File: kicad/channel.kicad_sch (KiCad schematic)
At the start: 20 parts, among them U1 OPA1678IDR

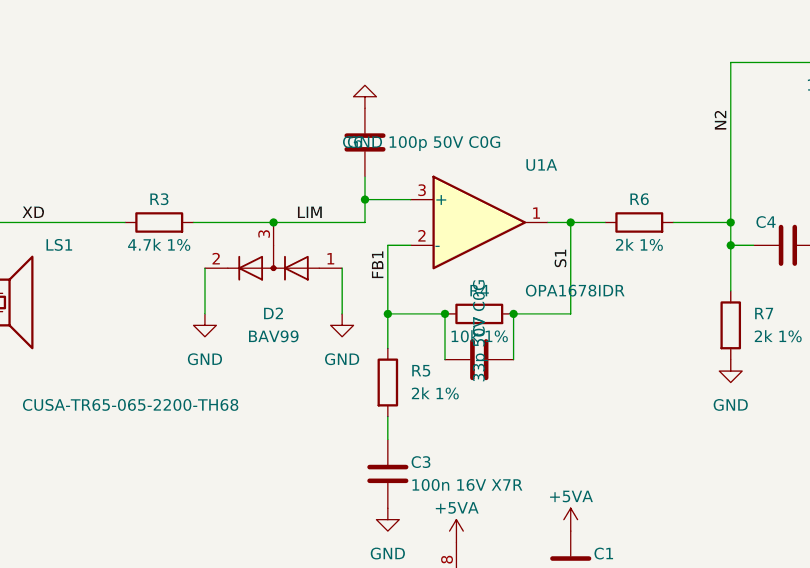
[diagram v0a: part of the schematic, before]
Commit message: AD7606C-16, one sheet per repeated block, clock buffering, first simulations
- ADC: AD7606C-16 in software mode (OS pins high, WR held high, DB11/SDI on
  shared ADC_SDI), 33 R source resistors on DOUTA/DOUTB/BUSY.
- Every repeated block is its own reused sheet: tx_group x16, en_buf x4,
  clk_buf x7, mic x8 (replaces tx_shift, tx_drivers, mems). Sheets other than
  channel are generated by scripts/build_cells.py and scripts/build_power.py.
- Headers: GND conductors either side of every clock, ADC_SDI, idle pulls,
  DNP RC terminations as fallback.
- Power: 3V3_MIC ferrite filter moved to the power sheet with LED, test point
  and flag.
- Simulations (LTspice, sim/): RX chain gain/noise, TX burst and recovery,
  clock signal integrity; results in docs/simulation-1.md. FPGA ribbon outputs
  changed to DRIVE 4 after simulation.
- Brief, CLAUDE.md, review status and SKiDL reference spec updated.
  ERC: 0 violations, 1,701 parts.
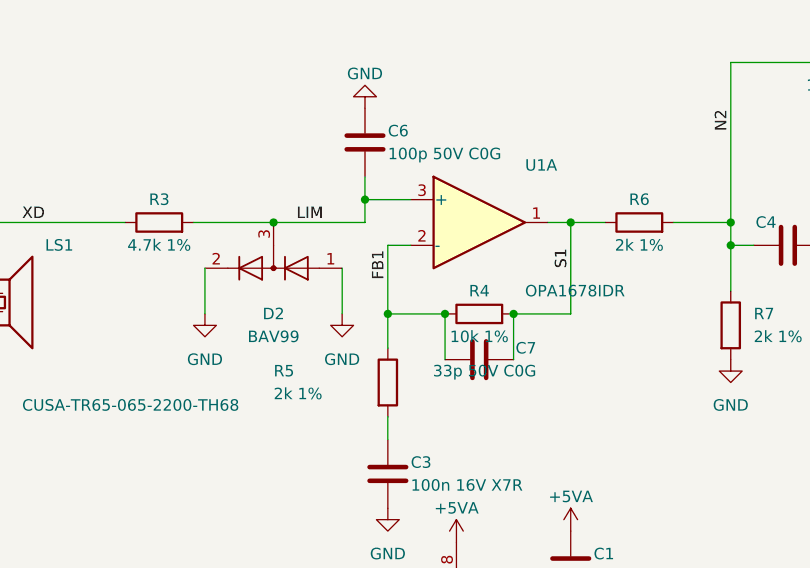
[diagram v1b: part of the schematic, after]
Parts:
- C6, C7: LCSC (none) -> TBD

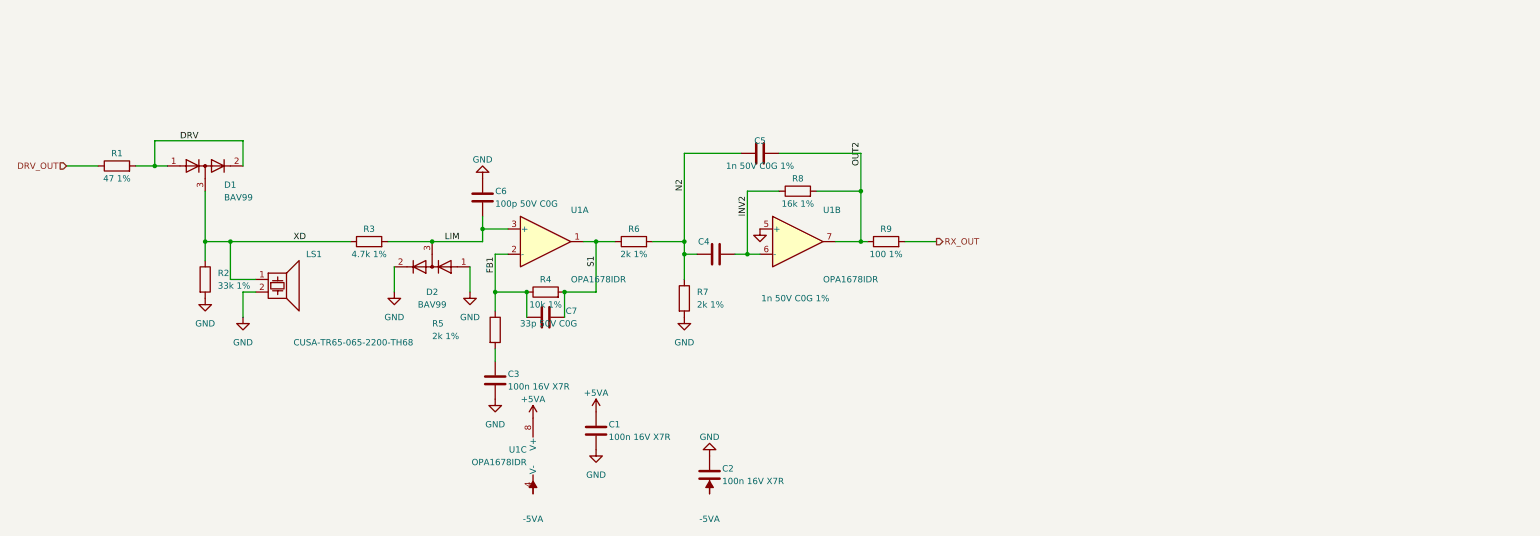
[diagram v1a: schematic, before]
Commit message: Block-diagram top page, power review fixes, readable sheets
Top level
- Page 1 is now a block diagram of the signal flow (FPGA -> headers ->
  clock buffers / TX drive -> transceivers -> ADCs -> FPGA, mics, power).
- New group sheets hold the reused cells: tx (16 tx_group + 4 en_buf),
  array (64 channel), adcs (8 adc), mics (8 mic), clocks (7 clk_buf).
  Power and headers stay directly under the top. All written by gen_top.py,
  which now also survives a kicad-cli re-save of a cell sheet.

Power (review findings)
- Polyfuse 1812L200/16DR (16 V), TPS65131RGER stated explicitly, input caps
  2 x 10u 1206, 50 V caps on 12 V, inductor values carry minimum Isat.
- +3V3: TLV75733P (ceramic-stable) replaces TLV1117-33.
- New JP5/JP6 isolate +-6V5; every rail: REG node -> jumper -> rail with TP,
  LED (not on analog LDOs) and PWR_FLAG.
- Power sheet is now generated by build_cells.py in a 2x3 block layout
  (build_power.py removed).

Readability and small fixes
- Rails on sideways pins use labelled flags; sideways GND symbols hide text.
- tx_group: 595 outputs wired straight to the drivers.
- Title blocks on every sheet; channel sheet notes and field placement fixed
  (sch_fields.py --only, sch_annotate.py).
- ADC_SDI 10k pull-down, ADC reset/DOUT notes, mic cap 50 V.
- ERC 0 violations, 1,704 parts. PDFs: docs/schematics/00..13.
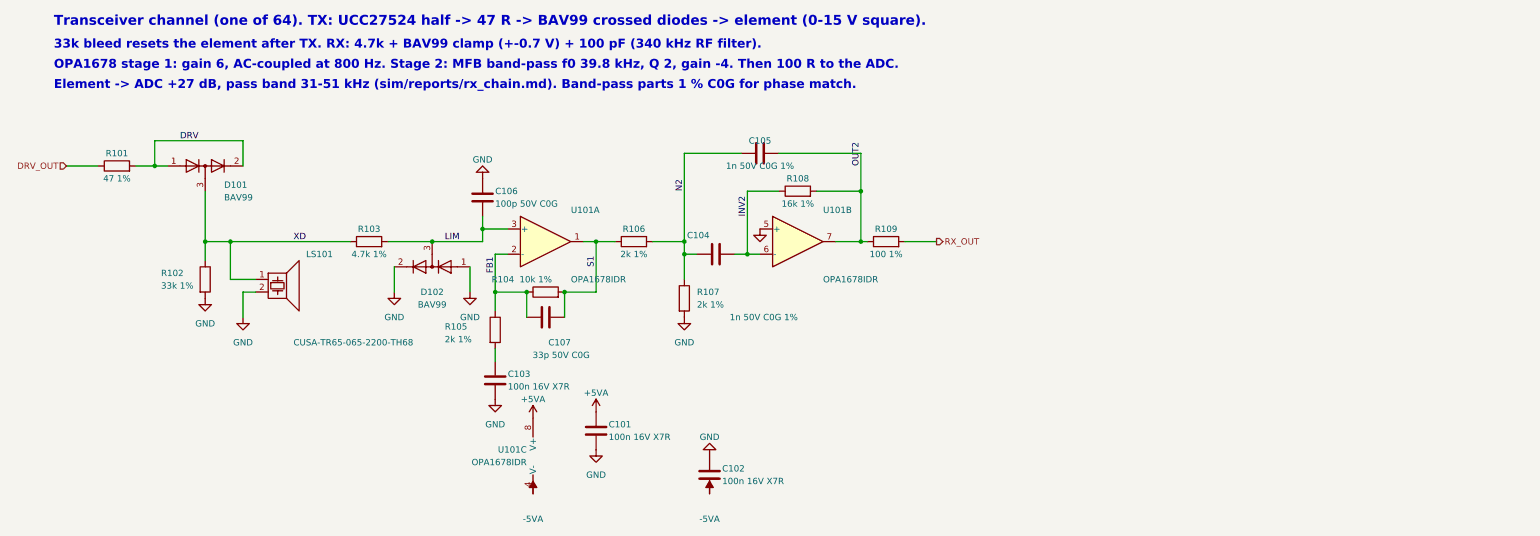
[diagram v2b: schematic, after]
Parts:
- renumbered C1 to C101, C2 to C102, C3 to C103, C4 to C104, C5 to C105, C6 to C106, C7 to C107, D1 to D101, D2 to D102, LS1 to LS101, R1 to R101, R2 to R102, R3 to R103, R4 to R104, R5 to R105, R6 to R106, R7 to R107, R8 to R108, R9 to R109, U1 to U101
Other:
- note added: "33k bleed resets the element after TX. RX: 4.7k + BAV99 clamp (+-0.7 V) + 100 pF (340 kHz RF filter)."
- note added: "Element -> ADC +27 dB, pass band 31-51 kHz (sim/reports/rx_chain.md). Band-pass parts 1 % C0G for phase match."
- note added: "OPA1678 stage 1: gain 6, AC-coupled at 800 Hz. Stage 2: MFB band-pass f0 39.8 kHz, Q 2, gain -4. Then 100 R to the ADC."
- note added: "Transceiver channel (one of 64). TX: UCC27524 half -> 47 R -> BAV99 crossed diodes -> element (0-15 V square)."
- company: (none) -> Hybrid 8x8 ultrasonic AESA
- title: (none) -> Transceiver channel (x64): TX, T/R switch, RX amplifier

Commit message: Optimized, costed BOM with LCSC numbers for every part
scripts/bom.py picks parts (Basic first, stock margin) and writes docs/bom.md,
fab/bom_jlcpcb.csv and scripts/parts.json; sch_lcsc.py fills LCSC fields from it.
Part changes: TPS7A4700RGWT for the out-of-stock TPS7A4701, BAV99 C2500, SS54 in SMA,
SMD1812P200TF16 polyfuse, 600R ferrite, Basic-value +5V/VDRV dividers (VDRV 15.4 V),
Sunlord SWPA6045 footprints, mic 100 nF C0G in 1206. AD7606C-16 and SPH0641 now
assembled by JLCPCB.
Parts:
- C101, C102, C103: LCSC TBD -> C14663
- C104, C105: LCSC TBD -> C309468
- C106: LCSC TBD -> C14858
- C107: LCSC TBD -> C1663
- D101, D102: LCSC C68983 -> C2500
- R101: LCSC TBD -> C23182
- R102: LCSC TBD -> C4216
- R103: LCSC TBD -> C23162
- R104: LCSC TBD -> C25804
- R105, R106, R107: LCSC TBD -> C22975
- R108: LCSC TBD -> C4210
- R109: LCSC TBD -> C22775
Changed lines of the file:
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@@
 			)
 		)
-		(property "LCSC" "C68983"
+		(property "LCSC" "C2500"
 			(at 101.6 71.12 0)
 			(hide yes)
@@
 			)
 		)
-		(property "LCSC" "TBD"
+		(property "LCSC" "C22775"
 			(at 193.04 66.04 0)
 			(hide yes)
@@
 			)
 		)
-		(property "LCSC" "TBD"
+		(property "LCSC" "C14858"
 			(at 111.76 57.15 0)
 			(hide yes)
@@
 			)
 		)
-		(property "LCSC" "TBD"
+		(property "LCSC" "C23182"
 			(at 38.1 50.8 0)
 			(hide yes)
@@
 			)
 		)
-		(property "LCSC" "TBD"
+		(property "LCSC" "C4216"
 			(at 55.88 73.66 0)
 			(hide yes)
@@
 			)
 		)
-		(property "LCSC" "TBD"
+		(property "LCSC" "C25804"
 			(at 124.46 76.2 0)
 			(hide yes)
@@
 			)
 		)
-		(property "LCSC" "TBD"
+		(property "LCSC" "C14663"
 			(at 157.48 113.03 0)
 			(hide yes)
@@
 			)
 		)
-		(property "LCSC" "TBD"
+		(property "LCSC" "C22975"
 			(at 114.3 83.82 0)
 			(hide yes)
@@
 			)
 		)
-		(property "LCSC" "TBD"
+		(property "LCSC" "C14663"
 			(at 114.3 93.98 0)
 			(hide yes)
@@
 			)
 		)
-		(property "LCSC" "C68983"
+		(property "LCSC" "C2500"
 			(at 55.88 50.8 0)
 			(hide yes)
@@
 			)
 		)
-		(property "LCSC" "TBD"
+		(property "LCSC" "C309468"
 			(at 167.64 48.26 0)
 			(hide yes)
@@
 			)
 		)
-		(property "LCSC" "TBD"
+		(property "LCSC" "C23162"
 			(at 88.9 66.04 0)
 			(hide yes)
@@
 			)
 		)
-		(property "LCSC" "TBD"
+		(property "LCSC" "C1663"
 			(at 124.46 81.28 0)
 			(hide yes)
@@
 			)
 		)
-		(property "LCSC" "TBD"
+		(property "LCSC" "C14663"
 			(at 134.62 104.14 0)
 			(hide yes)
@@
 			)
 		)
-		(property "LCSC" "TBD"
+		(property "LCSC" "C4210"
 			(at 175.26 55.88 0)
 			(hide yes)
@@
 			)
 		)
-		(property "LCSC" "TBD"
+		(property "LCSC" "C22975"
 			(at 152.4 77.47 0)
 			(hide yes)
@@
 			)
 		)
-		(property "LCSC" "TBD"
+		(property "LCSC" "C309468"
 			(at 158.75 68.58 0)
 			(hide yes)
@@
 			)
 		)
-		(property "LCSC" "TBD"
+		(property "LCSC" "C22975"
 			(at 142.24 66.04 0)
 			(hide yes)

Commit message: Switch to 16 x TLV320ADC5140, +3V3A rail, 3 A buck, datasheet library, transducer DNP
- ADC: 8 x AD7606C-16 ($470/board) -> 16 x TI TLV320ADC5140 at 192 kSPS ($50/board): TDM slave on a
  shared BCLK/FSYNC, I2C (SCL + 4 SDA groups), 2k/1k + 100 nF input network; project symbol from
  scripts/make_symbols.py; 9 clock buffers; J2 remapped
- power: +3V3A (second TPS7A4700, ANY-OUT 3.3 V); +5V buck TPS54202 -> TPS54302 (3 A), L1 10 uH 5 A
- checks and simulations updated for the new ADC input (all 18 checks and 10 sims pass)
- docs/datasheets: a PDF for every part, kept in step by scripts/datasheets.py (run by bom.py)
- design brief section 5a: interface bandwidth budget (no bus is a bottleneck; TX_EDGE = 1)
- CUSA-TR65 marked DNP for JLCPCB (hand-soldered), priced at DigiKey 100+
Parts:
- LS101: now not fitted
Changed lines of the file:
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@@
 		(on_board yes)
 		(in_pos_files yes)
-		(dnp no)
+		(dnp yes)
 		(property "Reference" "LS101"
 			(at 76.2 68.58 0)

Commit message: Transducer: Same Sky CUSP-TR80-15-2500-TH instead of CUSA-TR65 (about $122 less per board)
- Ø9.8 mm 40 kHz transceiver, 105 dB SPL, 0.2-15 m, 1.6 ms ring-down, 2.0 nF; $1.65 (Future,
  DigiKey second source); not sealed (indoor, behind the waveguide)
- new footprint aesa:CUSP-TR80 (5.0 mm pin pitch, Ø2 mm pads, Ø0.9 mm holes, '+' = pad 1);
  CUSA-TR65 footprint removed; soldering keep-out follows the larger pads
- simulation model CUSP_TR80 (C0 2.0 nF; Rm 3 k and the 1 m echo level kept as assumptions):
  all 10 simulations pass
- BOM total $326 per board (was $444); datasheet library, checks, brief and README updated;
  board re-placed, DRC 0 violations
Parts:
- LS101: value CUSA-TR65-065-2200-TH68 -> CUSP-TR80-15-2500-TH; footprint aesa:CUSA-TR65 -> aesa:CUSP-TR80
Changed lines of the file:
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@@
 			)
 		)
-		(property "Value" "CUSA-TR65-065-2200-TH68"
+		(property "Value" "CUSP-TR80-15-2500-TH"
 			(at 73.66 86.36 0)
 			(show_name no)
@@
 			)
 		)
-		(property "Footprint" "aesa:CUSA-TR65"
+		(property "Footprint" "aesa:CUSP-TR80"
 			(at 70.231 72.39 0)
 			(hide yes)
@@
 			)
 		)
-		(property "Sim.Name" "CUSA_TR65"
+		(property "Sim.Name" "CUSP_TR80"
 			(at 71.12 73.66 0)
 			(effects

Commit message: Board ready for routing: power sheets redrawn, 3D models, test access, routing setup
Schematic
- Power supply split into two boxed A3 sheets (Power 1: input, +5V, VDRV,
  +3V3, 3V3_MIC; Power 2: analog +-6V5, +-5VA, +3V3A and the bring-up notes);
  eFuse wired inline; text no longer clashes; ferrite drawn as L_Ferrite.
- Every page of the schematic PDF is A3 (cells scaled up, array redrawn).
- RX_OUT test pad on every channel; four more GND test points.
- Test pads and solder jumpers out of the BOM, like their footprints.

Board
- 3D model for every part (make_3d.py for the CUSP-TR80, stock substitutes
  for four missing library models); check_design checks it.
- JLC04161H-7628 stackup, ENIG; inner GND layers typed as planes; thermal
  reliefs on through-hole pads; HighCurrent net class (1 mm).
- Custom DRC rules (aesa.kicad_dru): TX/RX and switch-node separation,
  clock spacing, JLCPCB limits.
- Footprints keep their library IDs (schematic parity clean); assembly
  drawing docs/assembly/aesa_assembly.pdf.
- Freerouting 2.5.0 installed; DSN export checked.

ERC 0, DRC 0, design check 19/19, placement checks 12/12.
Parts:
- added TP101: RX, TestPoint:TestPoint_Pad_D1.0mm, symbol Connector:TestPoint
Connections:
- net RX_OUT: now also TP101.1

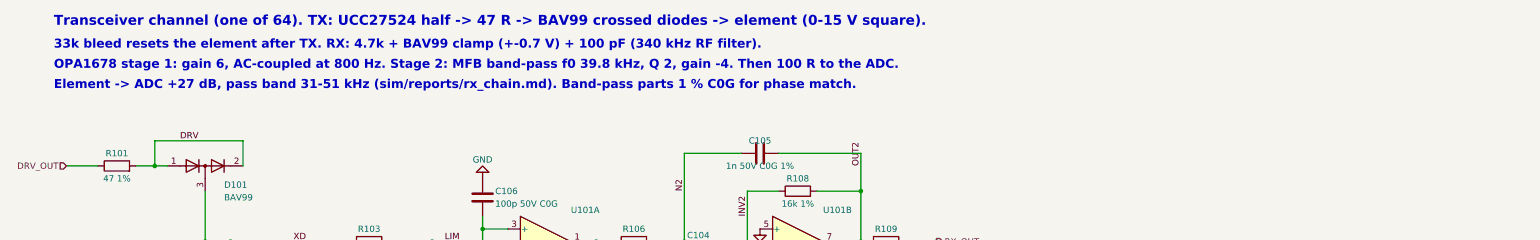
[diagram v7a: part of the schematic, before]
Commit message: Fix small inconsistencies: one revision (rev 1, 2026-10-24) for sheets and board
- REV/DATE come from scripts/common.py for every title block and the board
  silkscreen (the sheets said rev 2, the board rev 1).
- Channel note: +27 dB is element -> amplifier output; the ADC pin sees
  +16.5 dB after the divider.
- Board input text 8.8-13.8 V (eFuse UVLO); LM2731 limit 14 V (14.5 V abs max).
- Brief/README: real board size 192 x 301 mm, CUSP-TR80 footprint and pitch
  note, nominal vs simulated gain, board test-point references, 126 pages.
- SKiDL spec uses L_Ferrite like the sheet; dead AD7606/net-tie entries gone.

ERC 0, DRC 0, design check 19/19, placement checks 12/12.
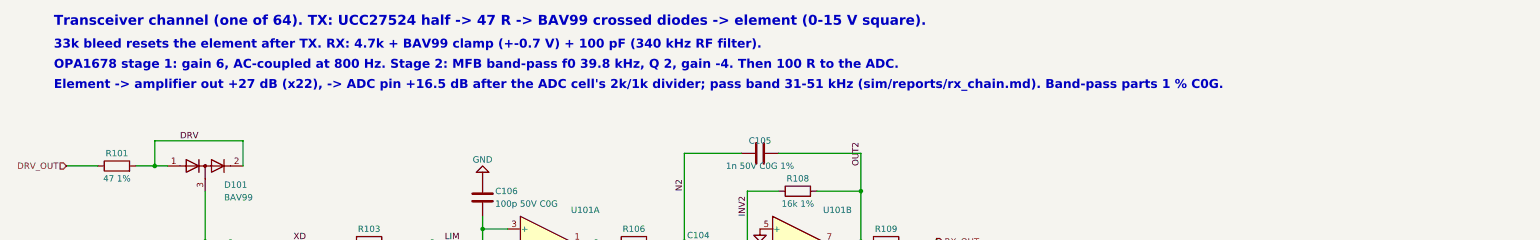
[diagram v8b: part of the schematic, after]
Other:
- note added: "Element -> amplifier out +27 dB (x22), -> ADC pin +16.5 dB after the ADC cell's 2k/1k divider; pass band 31-51 kHz (sim/reports/rx_chain.md). Band-pass parts 1 % C0G."
- note removed: "Element -> ADC +27 dB, pass band 31-51 kHz (sim/reports/rx_chain.md). Band-pass parts 1 % C0G for phase match."
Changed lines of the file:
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@@
 	(title_block
 		(title "Transceiver channel (x64): TX, T/R switch, RX amplifier")
-		(date "2026-10-20")
-		(rev "2")
+		(date "2026-10-24")
+		(rev "1")
 		(company "Hybrid 8x8 ultrasonic AESA")
 	)
-	(text "Transceiver channel (one of 64). TX: UCC27524 half -> 47 R -> BAV99 crossed diodes -> element (0-15 V square)."
-		(exclude_from_sim no)
-		(at 25.4 22.86 0)
-		(effects
-			(font
-				(size 2 2)
-				(bold yes)
-			)
-			(justify left bottom)
-		)
-	)
-	(text "33k bleed resets the element after TX. RX: 4.7k + BAV99 clamp (+-0.7 V) + 100 pF (340 kHz RF filter)."
-		(exclude_from_sim no)
-		(at 25.4 27.43 0)
-		(effects
-			(font
-				(size 1.8 1.8)
-				(bold yes)
-			)
-			(justify left bottom)
-		)
-	)
-	(text "OPA1678 stage 1: gain 6, AC-coupled at 800 Hz. Stage 2: MFB band-pass f0 39.8 kHz, Q 2, gain -4. Then 100 R to the ADC."
-		(exclude_from_sim no)
-		(at 25.4 31.5 0)
-		(effects
-			(font
-				(size 1.8 1.8)
-				(bold yes)
-			)
-			(justify left bottom)
-		)
-	)
-	(text "Element -> ADC +27 dB, pass band 31-51 kHz (sim/reports/rx_chain.md). Band-pass parts 1 % C0G for phase match."
-		(exclude_from_sim no)
-		(at 25.4 35.56 0)
-		(effects
-			(font
-				(size 1.8 1.8)
-				(bold yes)
-			)
-			(justify left bottom)
-		)
-	)
 	(junction
 		(at 114.3 76.2)
@@
 		)
 	)
+	(text "Transceiver channel (one of 64). TX: UCC27524 half -> 47 R -> BAV99 crossed diodes -> element (0-15 V square)."
+		(exclude_from_sim no)
+		(at 25.4 22.86 0)
+		(effects
+			(font
+				(size 2.0 2.0)
+				(bold yes)
+			)
+			(justify left bottom)
+		)
+	)
+	(text "33k bleed resets the element after TX. RX: 4.7k + BAV99 clamp (+-0.7 V) + 100 pF (340 kHz RF filter)."
+		(exclude_from_sim no)
+		(at 25.4 27.43 0)
+		(effects
+			(font
+				(size 1.8 1.8)
+				(bold yes)
+			)
+			(justify left bottom)
+		)
+	)
+	(text "OPA1678 stage 1: gain 6, AC-coupled at 800 Hz. Stage 2: MFB band-pass f0 39.8 kHz, Q 2, gain -4. Then 100 R to the ADC."
+		(exclude_from_sim no)
+		(at 25.4 31.5 0)
+		(effects
+			(font
+				(size 1.8 1.8)
+				(bold yes)
+			)
+			(justify left bottom)
+		)
+	)
+	(text "Element -> amplifier out +27 dB (x22), -> ADC pin +16.5 dB after the ADC cell's 2k/1k divider; pass band 31-51 kHz (sim/reports/rx_chain.md). Band-pass parts 1 % C0G."
+		(exclude_from_sim no)
+		(at 25.4 35.56 0)
+		(effects
+			(font
+				(size 1.8 1.8)
+				(bold yes)
+			)
+			(justify left bottom)
+		)
+	)
